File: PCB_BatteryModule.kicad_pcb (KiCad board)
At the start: 2 copper layers, 92 x 83 mm, 54 parts, among them J1 Interconnect A, J2 Interconnect B, J3 Debug, J4 Conn_01x04, Q1 IRF7406, Q2 IRF7469, U1 LM22679, U2 ACS712, U3 XMC1404_F064, U4 TLE7251, U5 LM35-D, U6 LM35-D

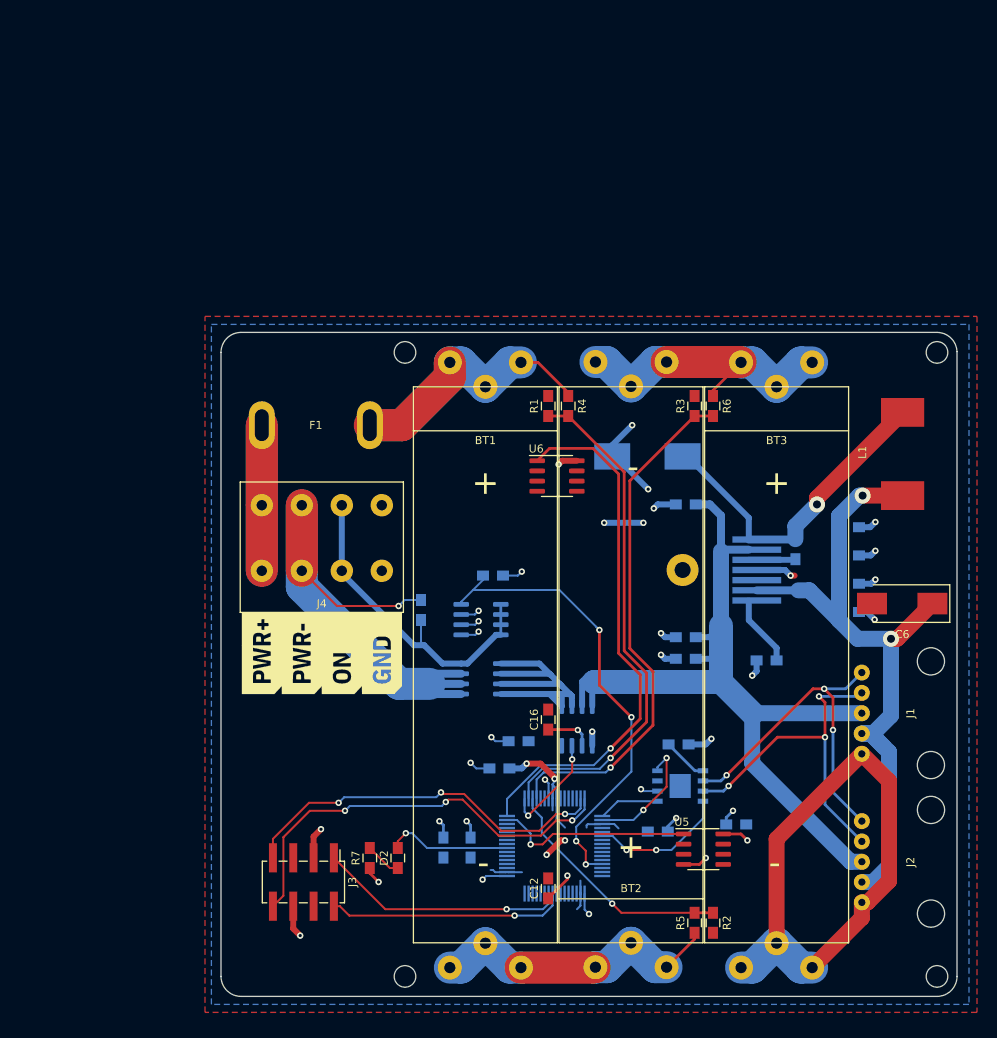
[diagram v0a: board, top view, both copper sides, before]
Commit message: Use AA Ni-Mh cells instead of 18650 Li-ion
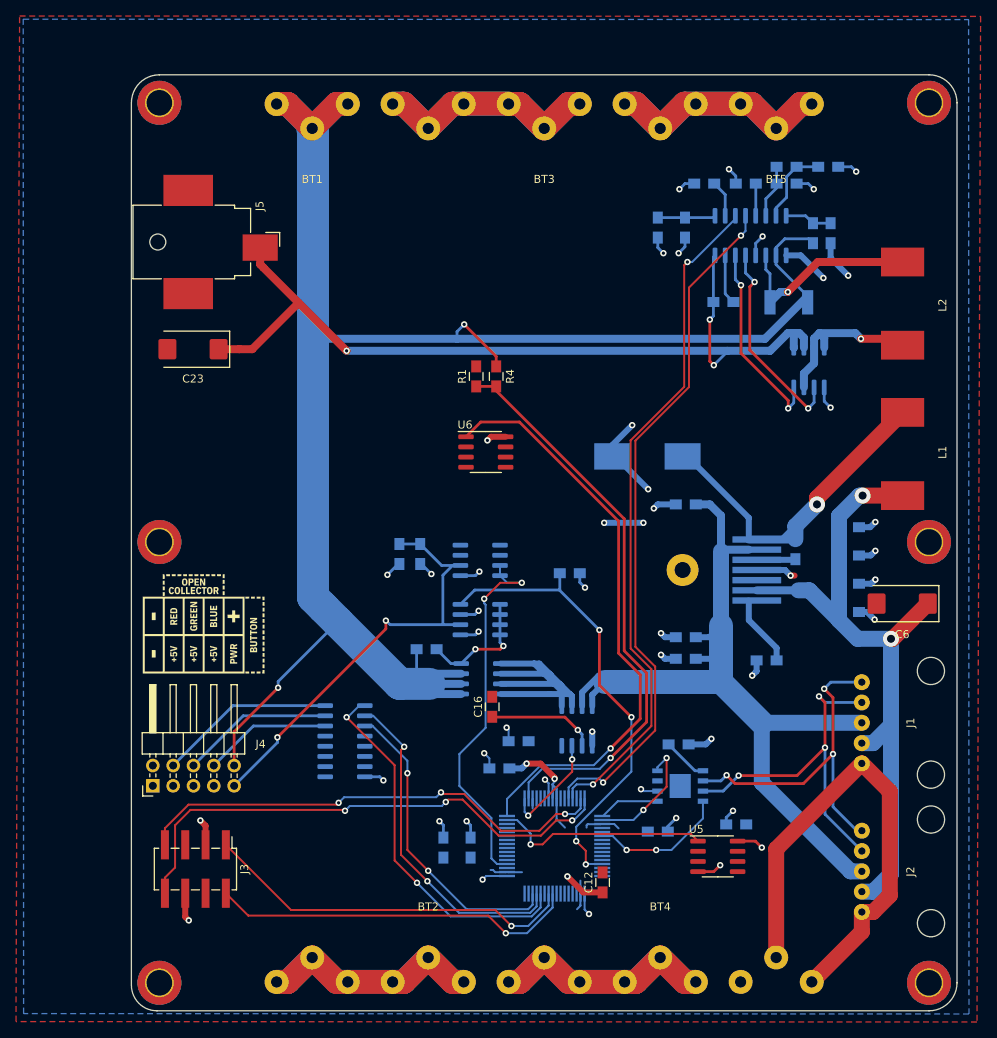
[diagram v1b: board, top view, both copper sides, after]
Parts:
- removed D2: LED, PCB_BatteryModule:C_0805_HandSoldering
- removed F1: Fuse, PCB_BatteryModule:Keystone_3557_Fuse_Holder
- removed the G*** at (109.0, 122.3)
- removed the G*** at (113.1, 98.1)
- removed R7: 1K2, PCB_BatteryModule:C_0805_HandSoldering
- removed the REF** at (123.5, 138.5)
- removed the REF** at (123.5, 60.5)
- removed the REF** at (190.0, 60.5)
- removed the REF** at (190.0, 138.5)
- added BT4: AA, PCB_BatteryModule:Battery_AA_THT_Keystone_590, F.Cu at (155.4, 136.1)
- added BT5: AA, PCB_BatteryModule:Battery_AA_THT_Keystone_590, F.Cu at (169.9, 32.5)
- added C20: 4.7uF, PCB_BatteryModule:C_0805_HandSoldering, B.Cu at (155.1, 44.9)
- added C21: 0.1uF, PCB_BatteryModule:C_0805_HandSoldering, B.Cu at (158.5, 44.9)
- added C22: 0.1uF, PCB_BatteryModule:C_0805_HandSoldering, B.Cu at (171.2, 39.4)
- added C23: 47uF, Capacitor_Tantalum_SMD:CP_EIA-7343-43_Kemet-X_Pad2.25x2.55mm_HandSolder, F.Cu at (97.0, 60.1)
- added C24: 0.01uF, PCB_BatteryModule:C_0805_HandSoldering, B.Cu at (166.1, 39.4)
- added C25: 0.33uF, PCB_BatteryModule:C_0805_HandSoldering, B.Cu at (163.3, 54.2)
- added G***: LOGO, PCB_BatteryModule:Pinout, F.Cu at (98.3, 94.4)
- added G***: LOGO, PCB_BatteryModule:Text_Wolley_BatteryECU_49mm_SilkScreen, B.Cu at (103.1, 65.4)
- added J5: Barrel_Jack, Connector_BarrelJack:BarrelJack_CUI_PJ-036AH-SMT_Horizontal, F.Cu at (99.6, 46.7)
- added L2: 47uH, PCB_BatteryModule:Inductor_SMD_Bourns_SRR1280, F.Cu at (185.7, 54.4)
- added Q3: IRF7303, Package_SO:SOIC-8_3.9x4.9mm_P1.27mm, B.Cu at (132.9, 86.5)
- added Q4: IRF7309, Package_SO:SOIC-8_3.9x4.9mm_P1.27mm, B.Cu at (174.0, 62.4)
- added R10: 68K, PCB_BatteryModule:C_0805_HandSoldering, B.Cu at (176.4, 37.3)
- added R11: 0.1, PCB_BatteryModule:C_2010_5025Metric_HandSoldering, B.Cu at (171.5, 54.2)
- added R12: 850K, PCB_BatteryModule:C_0805_HandSoldering, B.Cu at (174.5, 45.6)
- added R13: 100K, PCB_BatteryModule:C_0805_HandSoldering, B.Cu at (176.7, 45.6)
- added REF**: MountingHole_3.2mm_M3_ISO14580_Pad_TopBottom, MountingHole:MountingHole_3.2mm_M3_ISO14580_Pad_TopBottom, F.Cu at (92.8, 139.3)
- added REF**: MountingHole_3.2mm_M3_ISO14580_Pad_TopBottom, MountingHole:MountingHole_3.2mm_M3_ISO14580_Pad_TopBottom, F.Cu at (92.8, 84.2)
- added REF**: MountingHole_3.2mm_M3_ISO14580_Pad_TopBottom, MountingHole:MountingHole_3.2mm_M3_ISO14580_Pad_TopBottom, F.Cu at (189.0, 84.2)
- added REF**: MountingHole_3.2mm_M3_ISO14580_Pad_TopBottom, MountingHole:MountingHole_3.2mm_M3_ISO14580_Pad_TopBottom, F.Cu at (92.8, 29.3)
- added REF**: MountingHole_3.2mm_M3_ISO14580_Pad_TopBottom, MountingHole:MountingHole_3.2mm_M3_ISO14580_Pad_TopBottom, F.Cu at (189.0, 139.3)
- added REF**: MountingHole_3.2mm_M3_ISO14580_Pad_TopBottom, MountingHole:MountingHole_3.2mm_M3_ISO14580_Pad_TopBottom, F.Cu at (189.0, 29.3)
- added U7: MAX1640, Package_SO:SOIC-16_3.9x9.9mm_P1.27mm, B.Cu at (166.7, 45.9)
- added U8: ULN2003A, Package_SO:SOIC-16_3.9x9.9mm_P1.27mm, B.Cu at (116.0, 109.1)
- BT1, BT2, BT3: value 18650 -> AA; footprint PCB_BatteryModule:BatteryContact_THT_Keystone_590 -> PCB_BatteryModule:Battery_AA_THT_Keystone_590
- C17, C5: value 0.1uF -> 100nF
- C6: footprint Capacitors_Tantalum_SMD:CP_Tantalum_Case-X_EIA-7343-43_Hand -> Capacitor_Tantalum_SMD:CP_EIA-7343-43_Kemet-X_Pad2.25x2.55mm_HandSolder
- J1, J2: footprint PCB_BatteryModule:WolletInterconnect_THT_Angeled -> PCB_BatteryModule:WolleyInterconnect_THT_Angeled
- J4: value Conn_01x04 -> Button/Status; footprint PCB_BatteryModule:WAGO_2604-1104_PCB_Terminal_Block_4-Way -> Connector_PinHeader_2.54mm:PinHeader_2x05_P2.54mm_Horizontal
- Q2: value IRF7469 -> IRF7303
- R2, R3: value 2K -> 380K; moved to B.Cu
- R5: value 18K -> 23K3; moved to B.Cu
- R6: value 18K -> 200K; moved to B.Cu
- U1: value LM22679 -> LM22679-5.0
- U2: value ACS712 -> MCS1803GS-05P
- moved R5 92.4 mm to (160.9, 39.4), turned to 0 degrees
- moved R2 47.2 mm to (144.1, 88.1), turned to 0 degrees
- moved G*** 45.5 mm to (97.5, 69.9)
- moved BT3 43.4 mm to (140.9, 32.5)
- moved R3 41.3 mm to (122.8, 85.7), turned to 270 degrees
- moved BT1 38.9 mm to (111.9, 32.5)
- moved J4 37.5 mm to (92.0, 114.7), turned to 90 degrees
- moved R6 31.3 mm to (171.2, 37.3), turned to 180 degrees
- moved BT2 25.4 mm to (126.4, 136.1)
- moved J3 13.6 mm to (97.3, 125.1)
- moved R1 9.73 mm to (132.4, 63.5)
- moved R4 9.73 mm to (134.9, 63.5)
- moved R9 9.49 mm to (125.4, 85.7), turned to 270 degrees
- moved U6 9.39 mm to (133.6, 73.0)
- moved C16 7.18 mm to (134.4, 104.8)
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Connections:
- BT1 pad 1: Net-(BT1-Pad1) -> +BATT
- BT3 pad 2: -BATT -> Net-(BT3-Pad2)
- C1 pad 1: +BATT -> VDC
- C2 pad 1: +BATT -> VDC
- C3 pad 1: +BATT -> VDC
- J1 pad 3: +BATT -> VDC
- J2 pad 3: +BATT -> VDC
- J4 pad 1: Net-(F1-Pad1) -> -BATT
- J4 pad 2: Net-(J4-Pad2) -> -BATT
- J4 pad 3: Net-(J4-Pad3) -> +5V
- J4 pad 4: -BATT -> STATUS_RGB_RED_C
- Q1 pad 1: Net-(J4-Pad2) -> +BATT
- Q1 pad 2: Net-(J4-Pad2) -> +BATT
- Q1 pad 3: Net-(J4-Pad2) -> +BATT
- Q1 pad 4: Net-(J4-Pad3) -> Net-(Q1-Pad4)
- Q2 pad 2: -BATT -> Net-(J4-Pad9)
- Q2 pad 5: Net-(J4-Pad3) -> Net-(Q1-Pad4)
- Q2 pad 6: Net-(J4-Pad3) -> Net-(Q1-Pad4)
- Q2 pad 7: Net-(J4-Pad3) -> Net-(Q1-Pad4)
- Q2 pad 8: Net-(J4-Pad3) -> Net-(Q1-Pad4)
- R2 pad 1: V_BAT2 -> MAIN_POWER_ON
- R3 pad 1: V_BAT3 -> Net-(J4-Pad9)
- R4 pad 1: Net-(BT1-Pad1) -> +BATT
- R5 pad 1: Net-(BT1-Pad2) -> -BATT
- R5 pad 2: V_BAT2 -> Net-(R5-Pad2)
- R6 pad 1: Net-(BT2-Pad2) -> Net-(R10-Pad2)
- R6 pad 2: V_BAT3 -> Net-(C22-Pad2)
- R8 pad 1: Net-(J4-Pad3) -> Net-(Q1-Pad4)
- R8 pad 2: Net-(J4-Pad2) -> +BATT
- R9 pad 1: MAIN_POWER_ON -> Net-(J4-Pad9)
- U1 pad 2: +BATT -> VDC
- U2 pad 3: +BATT -> VDC
- U2 pad 4: +BATT -> VDC
- U3 pad 19: V_BAT2 -> Net-(U3-Pad19)
- U3 pad 20: V_BAT3 -> Net-(U3-Pad20)
- U3 pad 28: Net-(U3-Pad28) -> CHG_D0
- U3 pad 29: Net-(U3-Pad29) -> CHG_D1
- U3 pad 4: Net-(U3-Pad4) -> BUTTON
- U3 pad 60: Net-(U3-Pad60) -> STATUS_RGB_RED
- U3 pad 61: Net-(U3-Pad61) -> STATUS_RGB_GREEN
- U3 pad 62: Net-(U3-Pad62) -> STATUS_RGB_BLUE
- U3 pad 8: STATUS_LED -> Net-(U3-Pad8)
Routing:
- net +BATT: track 105.3 -> 240.1 mm, vias 0 -> 2
- net Net-(C23-Pad1): track 0.00 -> 108.3 mm, vias 0 -> 3
- net VDC: track 0.00 -> 105.1 mm
- net Net-(J4-Pad2): track 96.2 -> 0.00 mm, vias 1 -> 0
- net CHG_D0: track 0.00 -> 86.6 mm, vias 0 -> 2
- net CHG_D1: track 0.00 -> 85.0 mm, vias 0 -> 2
- net V_BAT3: track 65.2 -> 0.00 mm, vias 1 -> 0
- net Net-(J4-Pad9): track 0.00 -> 64.4 mm, vias 0 -> 2
- net Net-(BT3-Pad2): track 0.00 -> 56.9 mm
- net Net-(BT4-Pad2): track 0.00 -> 56.9 mm
- net Net-(BT1-Pad1): track 48.0 -> 0.00 mm
- net BUTTON: track 0.00 -> 47.7 mm, vias 0 -> 2
- net STATUS_RGB_RED: track 0.00 -> 46.6 mm, vias 0 -> 2
- net STATUS_RGB_GREEN: track 0.00 -> 42.1 mm, vias 0 -> 2
- net Net-(J4-Pad3): track 41.7 -> 0.00 mm
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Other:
- board size 92 x 83 mm -> 103.2 x 117 mm

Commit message: Version 2.0 with a lot of improvements
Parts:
- added D2: LED, LED_SMD:LED_0805_2012Metric_Pad1.15x1.40mm_HandSolder, F.Cu at (100.4, 75.2)
- added D3: LED, LED_SMD:LED_0805_2012Metric_Pad1.15x1.40mm_HandSolder, F.Cu at (100.4, 71.8)
- added D4: LED, LED_SMD:LED_0805_2012Metric_Pad1.15x1.40mm_HandSolder, F.Cu at (100.4, 68.4)
- added G***: LOGO, PCB_BatteryModule:Battery_AA_Symbol_SilkScreen, F.Cu at (169.9, 55.0)
- added G***: LOGO, PCB_BatteryModule:Battery_AA_Symbol_SilkScreen, F.Cu at (169.9, 113.5)
- added G***: LOGO, PCB_BatteryModule:Battery_AA_Symbol_SilkScreen, F.Cu at (126.4, 56.2)
- added G***: LOGO, PCB_BatteryModule:Battery_AA_Symbol_SilkScreen, F.Cu at (126.4, 114.7)
- added G***: LOGO, PCB_BatteryModule:Battery_AA_Symbol_SilkScreen, F.Cu at (112.0, 113.6)
- added G***: LOGO, PCB_BatteryModule:Battery_AA_Symbol_SilkScreen, F.Cu at (112.0, 55.1)
- added G***: LOGO, PCB_BatteryModule:Battery_AA_Symbol_SilkScreen, F.Cu at (140.9, 113.6)
- added G***: LOGO, PCB_BatteryModule:Battery_AA_Symbol_SilkScreen, F.Cu at (140.9, 55.1)
- added G***: LOGO, PCB_BatteryModule:Battery_AA_Symbol_SilkScreen, F.Cu at (155.4, 56.2)
- added G***: LOGO, PCB_BatteryModule:Battery_AA_Symbol_SilkScreen, F.Cu at (155.4, 114.7)
- added R14: 10K, PCB_BatteryModule:C_0805_HandSoldering, B.Cu at (103.0, 92.9)
- added R15: 10K, PCB_BatteryModule:C_0805_HandSoldering, B.Cu at (99.8, 90.4)
- added R16: 18K, PCB_BatteryModule:C_0805_HandSoldering, B.Cu at (162.8, 65.4)
- added R17: 2K, PCB_BatteryModule:C_0805_HandSoldering, B.Cu at (165.3, 65.4)
- added R7: 10K, PCB_BatteryModule:C_0805_HandSoldering, B.Cu at (106.3, 95.4)
- added SW1: SW_Push, Button_Switch_SMD:SW_SPST_Omron_B3FS-100xP, F.Cu at (94.8, 72.2)
- G***: moved to B.Cu
- U1: footprint TO_SOT_Packages_SMD:TO-263-7_TabPin8 -> Package_TO_SOT_SMD:TO-263-7_TabPin8
- U7: footprint Package_SO:SOIC-16_3.9x9.9mm_P1.27mm -> Package_SO:QSOP-16_3.9x4.9mm_P0.635mm
- moved G*** 32.4 mm to (99.9, 126.8), turned to 90 degrees
- moved G*** 25.9 mm to (94.2, 95.5)
- moved C16 15.7 mm to (149.3, 109.9), turned to 270 degrees
- moved J4 10.6 mm to (102.6, 114.6), turned to 180 degrees
- moved C20 3.49 mm to (158.2, 43.3), turned to 180 degrees
- moved C5 3.43 mm to (167.8, 95.7), turned to 180 degrees
- moved C3 3.24 mm to (161.8, 80.2)
- moved G*** 2.52 mm to (103.0, 62.9)
- moved C22 2.10 mm to (171.2, 37.3)
- moved R10 2.10 mm to (176.4, 39.4)
- moved R6 2.10 mm to (171.2, 39.4)
- moved R11 2.00 mm to (170.7, 52.4), turned to 90 degrees
- moved U7 1.65 mm to (165.1, 45.9)
- moved C13 0.86 mm to (129.2, 122.4)
- moved C4 0.80 mm to (171.5, 85.1)
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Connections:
- J4 pad 3: +5V -> STATUS_RGB_BLUE_C
- J4 pad 4: STATUS_RGB_RED_C -> +5V
- J4 pad 5: +5V -> STATUS_RGB_GREEN_C
- J4 pad 6: STATUS_RGB_GREEN_C -> +5V
- J4 pad 7: +5V -> STATUS_RGB_RED_C
- J4 pad 8: STATUS_RGB_BLUE_C -> +5V
- U3 pad 30: Net-(U3-Pad30) -> CHARGER_CONNECTED
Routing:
- net CHARGER_CONNECTED: track 0.00 -> 64.4 mm, vias 0 -> 2
- net Net-(J4-Pad9): track 64.4 -> 98.2 mm, vias 2 -> 4
- net +5V: track 140.5 -> 164.3 mm, vias 9 -> 12
- net Net-(D4-Pad1): track 0.00 -> 23.1 mm, vias 0 -> 1
- net Net-(D3-Pad1): track 0.00 -> 22.9 mm, vias 0 -> 1
- net Net-(D2-Pad1): track 0.00 -> 21.8 mm, vias 0 -> 1
- net STATUS_RGB_BLUE_C: track 16.0 -> 35.2 mm, vias 0 -> 1
- net +BATT: track 240.1 -> 254.7 mm, vias 2 -> 3
- net STATUS_RGB_GREEN_C: track 19.0 -> 28.2 mm, vias 0 -> 1
- net -BATT: track 182.8 -> 190.3 mm
- net MAIN_POWER_ON: track 58.7 -> 64.5 mm
- net Net-(C16-Pad1): track 13.7 -> 7.90 mm
- net V_BAT1: track 72.1 -> 66.6 mm
- net Net-(C5-Pad2): track 8.93 -> 4.20 mm
- net TEMP_SENSOR_2: track 73.7 -> 69.0 mm
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
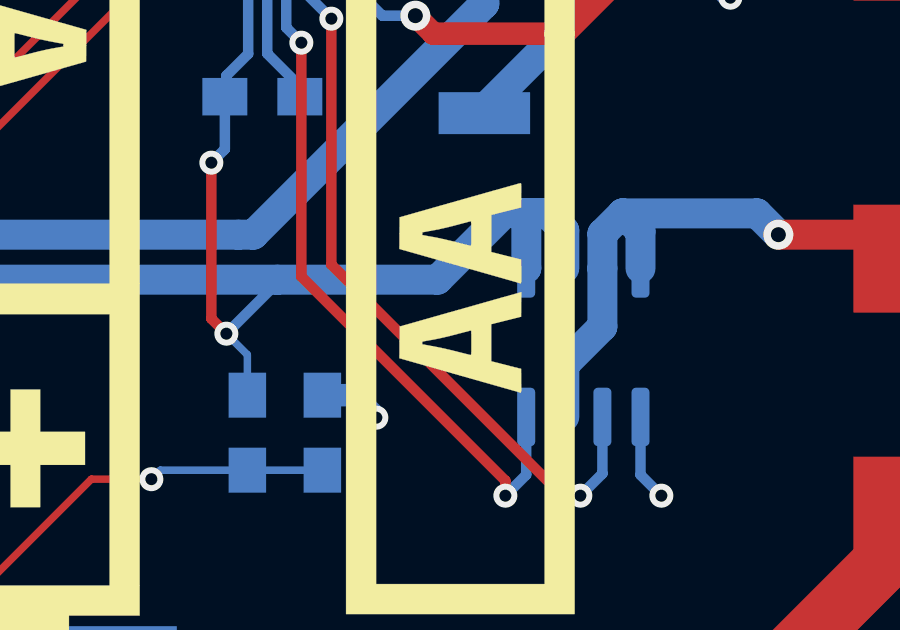
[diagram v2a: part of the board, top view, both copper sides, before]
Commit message: Fix bug in the charger circuit where the P-channel mosfet was connected mirrored
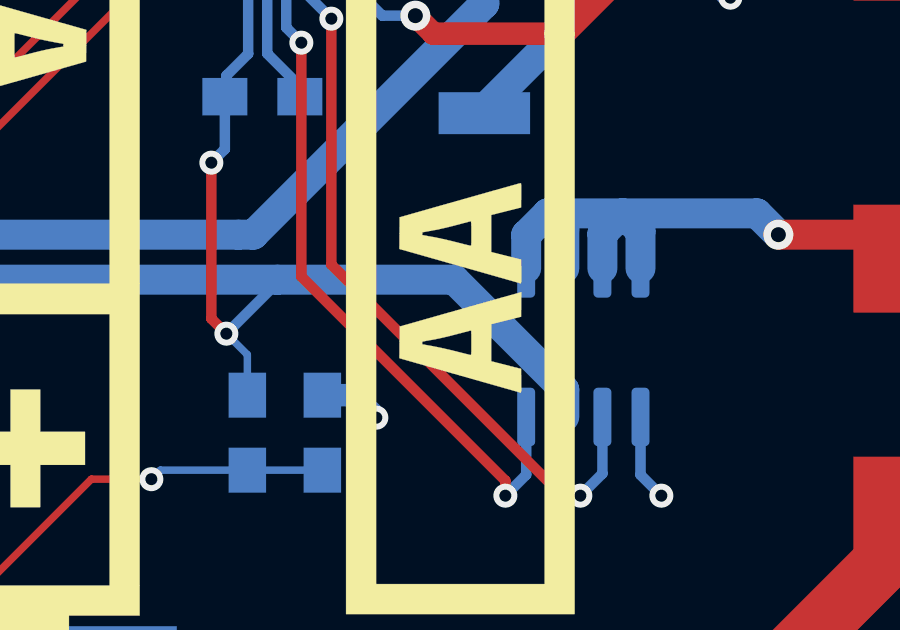
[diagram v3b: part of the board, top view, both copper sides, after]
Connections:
- Q4 pad 3: Net-(L2-Pad1) -> Net-(C23-Pad1)
- Q4 pad 5: Net-(C23-Pad1) -> Net-(L2-Pad1)
- Q4 pad 6: Net-(C23-Pad1) -> Net-(L2-Pad1)
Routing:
- net Net-(C23-Pad1): track 110.7 -> 108.9 mm
- net Net-(L2-Pad1): track 20.7 -> 21.9 mm
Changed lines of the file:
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@@
     (thickness 1.6)
     (drawings 13)
-    (tracks 876)
+    (tracks 873)
     (zones 0)
     (modules 90)
@@
   )
   (page A4)
+  (title_block
+    (date 2022-10-13)
+  )
   (layers
     (0 F.Cu signal)
@@
     (35 F.Paste user)
     (36 B.SilkS user)
-    (37 F.SilkS user)
+    (37 F.SilkS user hide)
     (38 B.Mask user)
     (39 F.Mask user)
@@
   )
   (setup
-    (last_trace_width 0.25)
+    (last_trace_width 1)
     (user_trace_width 0.35)
     (user_trace_width 0.75)
@@
       (net 83 "Net-(Q4-Pad2)"))
     (pad 3 smd roundrect (at -2.475 -0.635 90) (size 1.95 0.6) (layers B.Cu B.Paste B.Mask) (roundrect_rratio 0.25)
-      (net 79 "Net-(L2-Pad1)"))
+      (net 78 "Net-(C23-Pad1)"))
     (pad 4 smd roundrect (at -2.475 -1.905 90) (size 1.95 0.6) (layers B.Cu B.Paste B.Mask) (roundrect_rratio 0.25)
       (net 84 "Net-(Q4-Pad4)"))
     (pad 5 smd roundrect (at 2.475 -1.905 90) (size 1.95 0.6) (layers B.Cu B.Paste B.Mask) (roundrect_rratio 0.25)
-      (net 78 "Net-(C23-Pad1)"))
+      (net 79 "Net-(L2-Pad1)"))
     (pad 6 smd roundrect (at 2.475 -0.635 90) (size 1.95 0.6) (layers B.Cu B.Paste B.Mask) (roundrect_rratio 0.25)
-      (net 78 "Net-(C23-Pad1)"))
+      (net 79 "Net-(L2-Pad1)"))
     (pad 7 smd roundrect (at 2.475 0.635 90) (size 1.95 0.6) (layers B.Cu B.Paste B.Mask) (roundrect_rratio 0.25)
       (net 79 "Net-(L2-Pad1)"))
@@
   (segment (start 105.8 49.9) (end 110.2 54.3) (width 1) (layer F.Cu) (net 78))
   (segment (start 102.8 60.1) (end 100.2 60.1) (width 1) (layer F.Cu) (net 78))
-  (segment (start 172.78 58.08) (end 173.365 58.665) (width 1) (layer B.Cu) (net 78))
-  (segment (start 173.365 58.665) (end 173.365 59.925) (width 1) (layer B.Cu) (net 78))
-  (segment (start 169.14 60.3) (end 171.36 58.08) (width 1) (layer B.Cu) (net 78))
-  (segment (start 163.8 60.3) (end 169.14 60.3) (width 1) (layer B.Cu) (net 78))
-  (segment (start 172.1 59.92) (end 172.095 59.925) (width 1) (layer B.Cu) (net 78))
-  (segment (start 172.1 58.08) (end 172.1 59.92) (width 1) (layer B.Cu) (net 78))
-  (segment (start 171.36 58.08) (end 172.1 58.08) (width 1) (layer B.Cu) (net 78))
-  (segment (start 172.1 58.08) (end 172.78 58.08) (width 1) (layer B.Cu) (net 78))
   (segment (start 162.8 62.799998) (end 162.100002 62.1) (width 0.25) (layer B.Cu) (net 78))
   (segment (start 162.8 64.15) (end 162.8 62.799998) (width 0.25) (layer B.Cu) (net 78))
@@
   (segment (start 162.1 53.5) (end 162.1 54.15) (width 0.35) (layer B.Cu) (net 78))
   (segment (start 162.8275 48.5543) (end 162.8275 52.7725) (width 0.35) (layer B.Cu) (net 78))
+  (segment (start 173.365 63.967902) (end 173.365 64.875) (width 1) (layer B.Cu) (net 78))
+  (segment (start 169.697098 60.3) (end 173.365 63.967902) (width 1) (layer B.Cu) (net 78))
+  (segment (start 163.8 60.3) (end 169.697098 60.3) (width 1) (layer B.Cu) (net 78))
   (via (at 180.5 58.8) (size 1) (drill 0.5) (layers F.Cu B.Cu) (net 79))
   (segment (start 184.9 58.8) (end 185.7 59.6) (width 1) (layer F.Cu) (net 79))
   (segment (start 180.5 58.8) (end 184.9 58.8) (width 1) (layer F.Cu) (net 79))
-  (segment (start 173.365 63.135) (end 173.365 64.875) (width 1) (layer B.Cu) (net 79))
-  (segment (start 174.635 61.865) (end 173.365 63.135) (width 1) (layer B.Cu) (net 79))
-  (segment (start 174.635 59.925) (end 174.635 61.865) (width 1) (layer B.Cu) (net 79))
   (segment (start 174.635 58.765) (end 174.635 59.925) (width 1) (layer B.Cu) (net 79))
   (segment (start 175.31 58.09) (end 174.635 58.765) (width 1) (layer B.Cu) (net 79))
@@
   (segment (start 175.905 58.685) (end 175.31 58.09) (width 1) (layer B.Cu) (net 79))
   (segment (start 175.905 59.925) (end 175.905 58.685) (width 1) (layer B.Cu) (net 79))
+  (segment (start 172.81 58.09) (end 175.31 58.09) (width 1) (layer B.Cu) (net 79))
+  (segment (start 172.095 58.805) (end 172.81 58.09) (width 1) (layer B.Cu) (net 79))
+  (segment (start 172.095 59.925) (end 172.095 58.805) (width 1) (layer B.Cu) (net 79))
+  (segment (start 173.365 58.645) (end 172.81 58.09) (width 1) (layer B.Cu) (net 79))
+  (segment (start 173.365 59.925) (end 173.365 58.645) (width 1) (layer B.Cu) (net 79))
   (via (at 173.2 52.100002) (size 1) (drill 0.5) (layers F.Cu B.Cu) (net 80))
   (segment (start 185.7 49.2) (end 176.100002 49.2) (width 1) (layer F.Cu) (net 80))
